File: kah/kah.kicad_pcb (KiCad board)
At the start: 2 copper layers, 30 parts, among them X1 Клеммник_х2, X2 Клеммник_х2, X3 Клеммник_х2, X4 Клеммник_х2, X5 Клеммник_х2

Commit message: готова трассировка (50х55 мм)
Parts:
- added G***: LOGO, N_ICO:instagram_3x3, B.Cu at (114.5, 51.5)
- added G***: LOGO, N_ICO:ni_10x10, B.Cu at (109.8, 45.8)
- added G***: LOGO, N_ICO:ing-plus_13x13, F.Cu at (128.2, 61.8)
- added G***: LOGO, N_ICO:ni_10x10, F.Cu at (109.5, 46.8)
- added M3: Отверстие_М3, N_X:Отверстие_М3, F.Cu at (130.0, 72.0)
- C1, DD1, R1, R10, R11, R12, R13, R2, R3, R4, R5, R6, R7, R8, R9, VT1, VT2, VT3, VT4, VT5: moved to B.Cu
- moved R13 133.2 mm to (112.8, 62.0)
- moved R7 127.7 mm to (114.8, 74.8), turned to 180 degrees
- moved VT5 120.2 mm to (97.2, 70.2), turned to 180 degrees
- moved VT2 117.8 mm to (126.1, 81.5), turned to 180 degrees
- moved R10 114.1 mm to (112.8, 59.5)
- moved VT7 111.3 mm to (97.2, 66.2)
- moved VT6 97.9 mm to (97.2, 50.8)
- moved R11 96.4 mm to (112.8, 67.0)
- moved VT4 94.8 mm to (97.2, 55.5), turned to 180 degrees
- moved VT3 94.7 mm to (122.5, 62.9), turned to 270 degrees
- moved R12 93.9 mm to (112.8, 57.0)
- moved R3 92.9 mm to (112.8, 64.5)
- moved X4 91.4 mm to (87.5, 53.5), turned to 270 degrees
- moved R9 89.6 mm to (121.5, 49.5)
- moved DD1 87.3 mm to (131.2, 57.2), turned to 180 degrees
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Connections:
- R1 pad 2: /D4 -> /D2
- R10 pad 2: /D9 -> /D6
- R11 pad 2: /D6 -> /D3
- R12 pad 2: /D5 -> /D9
- R13 pad 2: /D3 -> /D5
- R3 pad 2: /D2 -> /D4
- VT1 pad 3: /D4 -> /D2
- VT2 pad 3: /D2 -> /D4
- VT4 pad 1: /D9 -> /D6
- VT4 pad 2: /DOut_1 -> /DOut_3
- VT5 pad 1: /D6 -> /D3
- VT5 pad 2: /DOut_2 -> /DOut_4
- VT6 pad 1: /D5 -> /D9
- VT6 pad 2: /DOut_3 -> /DOut_1
- VT7 pad 1: /D3 -> /D5
- VT7 pad 2: /DOut_4 -> /DOut_2
- X4 pad 1: /DOut_1 -> /DOut_3
- X4 pad 2: /DOut_2 -> /DOut_4
- X5 pad 1: /DOut_3 -> /DOut_1
- X5 pad 2: /DOut_4 -> /DOut_2
- XS2 pad 5: /RS_Z -> /RS_Y
- XS2 pad 6: /RS_Y -> /RS_Z
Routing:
- net /3V3: track 0.00 -> 70.0 mm
- net /5V: track 0.00 -> 57.1 mm, vias 0 -> 6
- net /D13_SCK: track 0.00 -> 54.0 mm, vias 0 -> 1
- net /D12_MISO: track 0.00 -> 49.3 mm, vias 0 -> 1
- net /D10_SS: track 0.00 -> 48.5 mm
- net /D11_MOSI: track 0.00 -> 47.4 mm, vias 0 -> 1
- net /D8_RES: track 0.00 -> 47.0 mm, vias 0 -> 2
- net /GND: track 0.00 -> 41.5 mm, vias 0 -> 9
- net /D7_IRQ: track 0.00 -> 36.3 mm
- net /D5: track 0.00 -> 32.4 mm, vias 0 -> 1
- net /D9: track 0.00 -> 31.4 mm, vias 0 -> 1
- net /RX: track 0.00 -> 30.9 mm, vias 0 -> 2
- net /D3: track 0.00 -> 27.6 mm
- net /D2: track 0.00 -> 26.1 mm, vias 0 -> 1
- net /D4: track 0.00 -> 25.9 mm, vias 0 -> 1
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- added copper zone on F.Cu, net /5V
- added copper zone on B.Cu, net /GND
- added copper zone on F.Cu, net /GND
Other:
- board outline added: 55 x 50 mm
- net class PWR added: clearance 0.2, trace_width 1, via_dia 0.8, via_drill 0.4
- board text added: "12V"
- board text added: "3V"
- board text added: "DI1"
- board text added: "DI2"
- board text added: "DO1"
- board text added: "DO2"
- board text added: "DO3"
- board text added: "DO4"
- board text added: "GND"
- board text added: "IRQ"
- board text added: "MISO"
- board text added: "MOSI"
- board text added: "RES"
- board text added: "SCK"
- board text added: "SS"
- board text added: "el.a.nikitos"
- board text added: "kah.0"
- board text added: "pcb@ing-plus.ru"

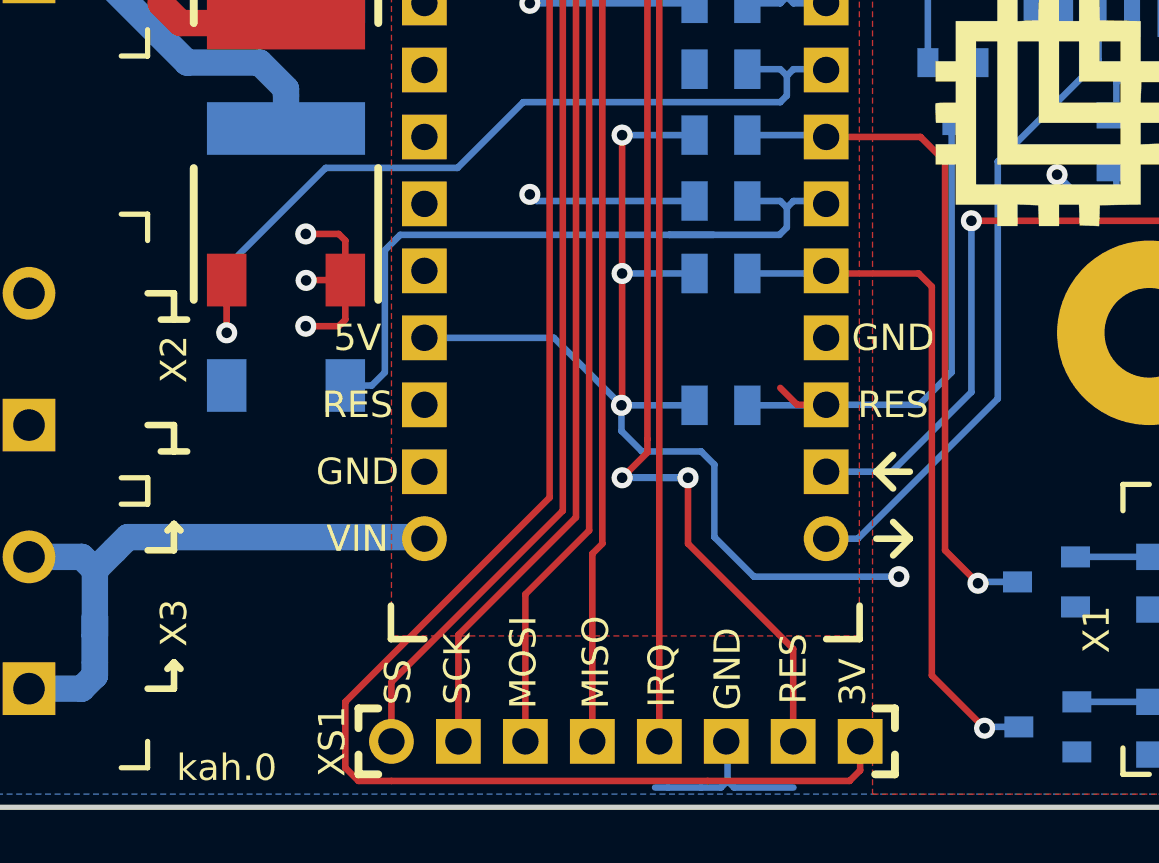
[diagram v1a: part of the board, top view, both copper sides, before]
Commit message: добавлено согласующее сопротивление на RX - изменена версия
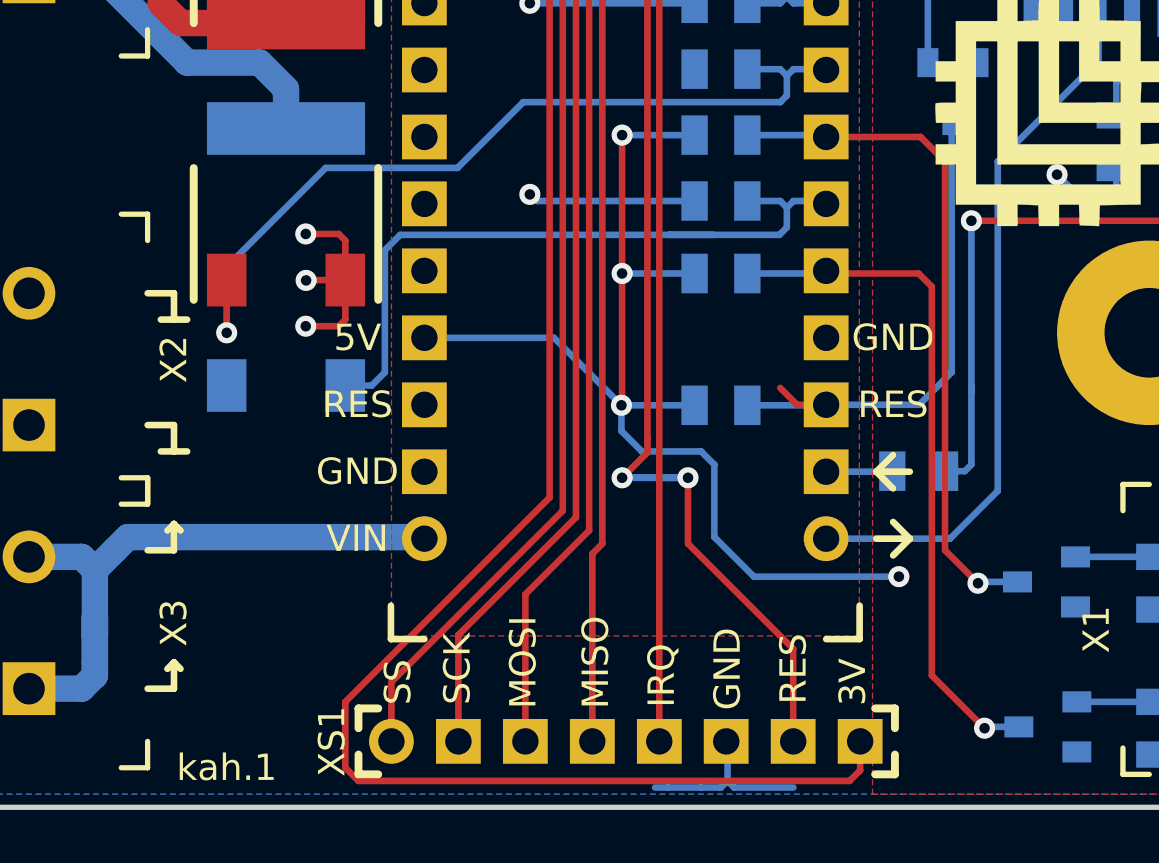
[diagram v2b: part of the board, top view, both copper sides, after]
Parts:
- added R14: 20k_0805, N_RLC:Резистор_SMD_0805_0,125Вт, B.Cu at (120.2, 77.2)
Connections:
- A1 pad 17: /RX -> Net-(A1-Pad17)
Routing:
- net /RX: track 30.9 -> 28.3 mm
- net Net-(A1-Pad17): track 0.00 -> 2.52 mm
- net /TX: track 24.8 -> 26.8 mm
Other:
- board text added: "kah.1"
- board text removed: "kah.0"
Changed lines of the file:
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@@
     (thickness 1.6)
     (drawings 44)
-    (tracks 320)
+    (tracks 323)
     (zones 0)
-    (modules 35)
-    (nets 46)
+    (modules 36)
+    (nets 47)
   )
   (page A4)
@@
   (net 44 /RS_Y)
   (net 45 "Net-(DD1-Pad8)")
+  (net 46 "Net-(A1-Pad17)")
   (net_class Default "Это класс цепей по умолчанию."
     (clearance 0.2)
@@
     (add_net "Net-(A1-Pad12)")
     (add_net "Net-(A1-Pad13)")
+    (add_net "Net-(A1-Pad17)")
     (add_net "Net-(A1-Pad3)")
     (add_net "Net-(A1-Pad5)")
@@
     (add_net /DOut_3)
     (add_net /DOut_4)
+  )
+  (module N_RLC:Резистор_SMD_0805_0,125Вт (layer B.Cu)
+    (at 120.25 77.25)
+    (fp_text reference R14 (at 1.25 -2) (layer B.SilkS)
+      (effects (font (size 1 1) (thickness 0.2)) (justify mirror))
+    )
+    (fp_text value 20k_0805 (at 1.29 -2.09) (layer B.Fab) hide
+      (effects (font (size 2 1.6) (thickness 0.3)) (justify mirror))
+    )
+    (fp_line (start 0.85 -0.2) (end 1.15 -0.45) (layer B.SilkS) (width 0.25))
+    (fp_line (start 0.85 0.45) (end 1.15 0.2) (layer B.SilkS) (width 0.25))
+    (fp_line (start -0.9 -1.1) (end -0.9 1.1) (layer B.SilkS) (width 0.25))
+    (fp_line (start 2.9 1.1) (end 2.9 -1.1) (layer B.SilkS) (width 0.25))
+    (fp_line (start -0.9 -1.1) (end 0.1 -1.1) (layer B.SilkS) (width 0.25))
+    (fp_line (start 2.9 -1.1) (end 1.9 -1.1) (layer B.SilkS) (width 0.25))
+    (fp_line (start 2.9 1.1) (end 1.9 1.1) (layer B.SilkS) (width 0.25))
+    (fp_line (start -0.9 1.1) (end 0.1 1.1) (layer B.SilkS) (width 0.25))
+    (pad 1 smd rect (at 0 0) (size 1 1.5) (layers B.Cu B.Paste B.Mask)
+      (net 46 "Net-(A1-Pad17)") (clearance 0.2))
+    (pad 2 smd rect (at 2 0) (size 1 1.5) (layers B.Cu B.Paste B.Mask)
+      (net 3 /RX) (clearance 0.2))
+    (model ${N_3D}/Res_0805.stp
+      (offset (xyz 0.05 0.61 0))
+      (scale (xyz 1 1 1))
+      (rotate (xyz 0 0 90))
+    )
   )
   (module N_ICO:instagram_3x3 (layer B.Cu)
@@
       (net 2 /12V))
     (pad 17 thru_hole rect (at 15.24 33.02) (size 1.7 1.7) (drill 1) (layers *.Cu *.Mask)
-      (net 3 /RX))
+      (net 46 "Net-(A1-Pad17)"))
     (pad 2 thru_hole rect (at 0 33.02) (size 1.7 1.7) (drill 1) (layers *.Cu *.Mask)
       (net 4 /GND))
@@
     )
   )
-  (gr_text kah.0 (at 95 88.5) (layer F.SilkS)
+  (gr_text kah.1 (at 95 88.5) (layer F.SilkS)
     (effects (font (size 1 1) (thickness 0.2)))
   )
@@
     (effects (font (size 1 1) (thickness 0.2)))
   )
-  (segment (start 118.942081 79.81) (end 124.25 74.502081) (width 0.25) (layer B.Cu) (net 1))
-  (segment (start 117.74 79.81) (end 118.942081 79.81) (width 0.25) (layer B.Cu) (net 1))
   (segment (start 128.075 61.675) (end 128.075 60.044) (width 0.25) (layer B.Cu) (net 1))
-  (segment (start 124.25 67) (end 124.25 65.5) (width 0.25) (layer B.Cu) (net 1))
-  (segment (start 124.25 74.502081) (end 124.25 67) (width 0.25) (layer B.Cu) (net 1))
+  (segment (start 124.25 78) (end 124.25 65.5) (width 0.25) (layer B.Cu) (net 1))
   (segment (start 124.25 65.5) (end 128.075 61.675) (width 0.25) (layer B.Cu) (net 1))
+  (segment (start 122.44 79.81) (end 124.25 78) (width 0.25) (layer B.Cu) (net 1))
+  (segment (start 117.74 79.81) (end 122.44 79.81) (width 0.25) (layer B.Cu) (net 1))
   (segment (start 90 82.75) (end 90 84.5) (width 1) (layer B.Cu) (net 2))
   (segment (start 90 85) (end 89.5 85.5) (width 1) (layer B.Cu) (net 2))
@@
   (segment (start 131.885 61.385) (end 133.25 62.75) (width 0.25) (layer B.Cu) (net 3))
   (segment (start 131.885 60.044) (end 131.885 61.385) (width 0.25) (layer B.Cu) (net 3))
-  (segment (start 117.74 77.27) (end 120.23 77.27) (width 0.25) (layer B.Cu) (net 3))
-  (segment (start 123.25 74.25) (end 123.25 67.75) (width 0.25) (layer B.Cu) (net 3))
   (via (at 123.25 67.75) (size 0.8) (drill 0.4) (layers F.Cu B.Cu) (net 3))
-  (segment (start 120.23 77.27) (end 123.25 74.25) (width 0.25) (layer B.Cu) (net 3))
   (segment (start 123.25 67.75) (end 132.25 67.75) (width 0.25) (layer F.Cu) (net 3))
   (segment (start 133.25 66.75) (end 133.25 62.75) (width 0.25) (layer F.Cu) (net 3))
   (segment (start 132.25 67.75) (end 133.25 66.75) (width 0.25) (layer F.Cu) (net 3))
+  (segment (start 122.25 77.25) (end 123 77.25) (width 0.25) (layer B.Cu) (net 3))
+  (segment (start 123.25 77) (end 123.25 74) (width 0.25) (layer B.Cu) (net 3))
+  (segment (start 123.25 74) (end 123.25 67.75) (width 0.25) (layer B.Cu) (net 3))
+  (segment (start 123 77.25) (end 123.25 77) (width 0.25) (layer B.Cu) (net 3))
+  (segment (start 123.25 74.25) (end 123.25 74) (width 0.25) (layer B.Cu) (net 3))
   (via (at 98.012653 70.012653) (size 0.8) (drill 0.4) (layers F.Cu B.Cu) (net 4))
   (segment (start 98.025306 70) (end 98.012653 70.012653) (width 0.25) (layer F.Cu) (net 4))
@@
   (segment (start 129.75 52) (end 130.5 51.25) (width 0.25) (layer B.Cu) (net 44))
   (segment (start 130.5 51.1) (end 130.5 50) (width 0.25) (layer B.Cu) (net 44))
+  (segment (start 117.74 77.27) (end 120.23 77.27) (width 0.25) (layer B.Cu) (net 46))
+  (segment (start 120.23 77.27) (end 120.25 77.25) (width 0.25) (layer B.Cu) (net 46))
   (zone (net 4) (net_name /GND) (layer B.Cu) (hatch edge 0.508)
     (connect_pads (clearance 0.5))
